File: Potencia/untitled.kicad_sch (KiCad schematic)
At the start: 13 parts, among them U3.3 LM2596S-3.3, U5 LM2596S-5

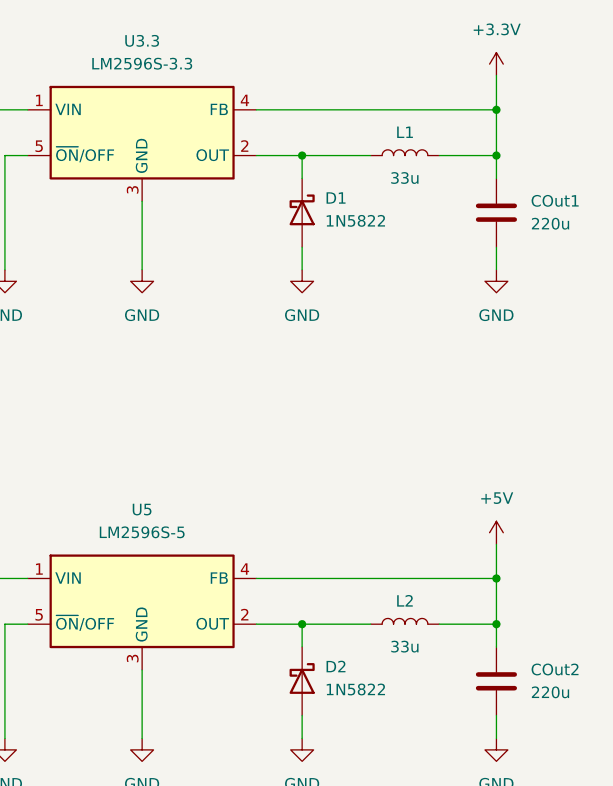
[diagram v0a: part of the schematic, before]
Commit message: correción de algunas referencias
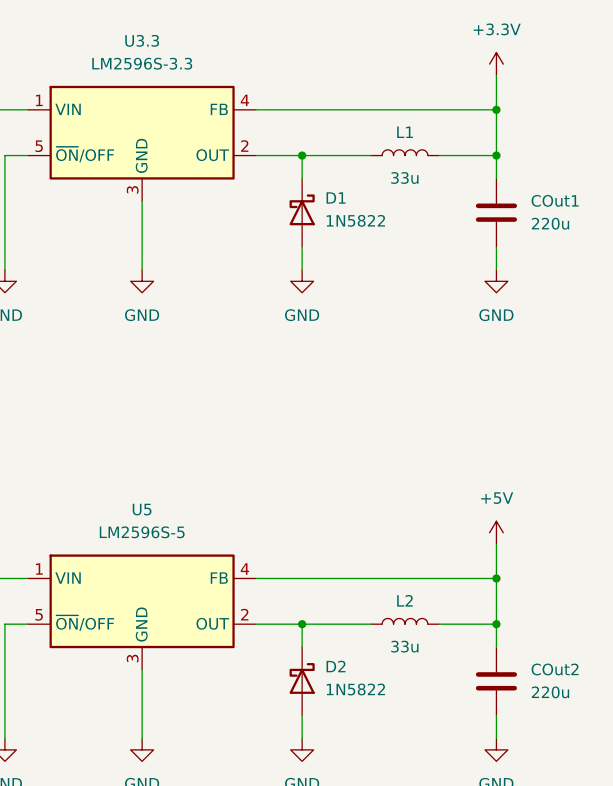
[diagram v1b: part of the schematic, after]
